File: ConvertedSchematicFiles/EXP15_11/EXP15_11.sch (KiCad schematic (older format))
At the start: 17 parts, among them U5 uA741

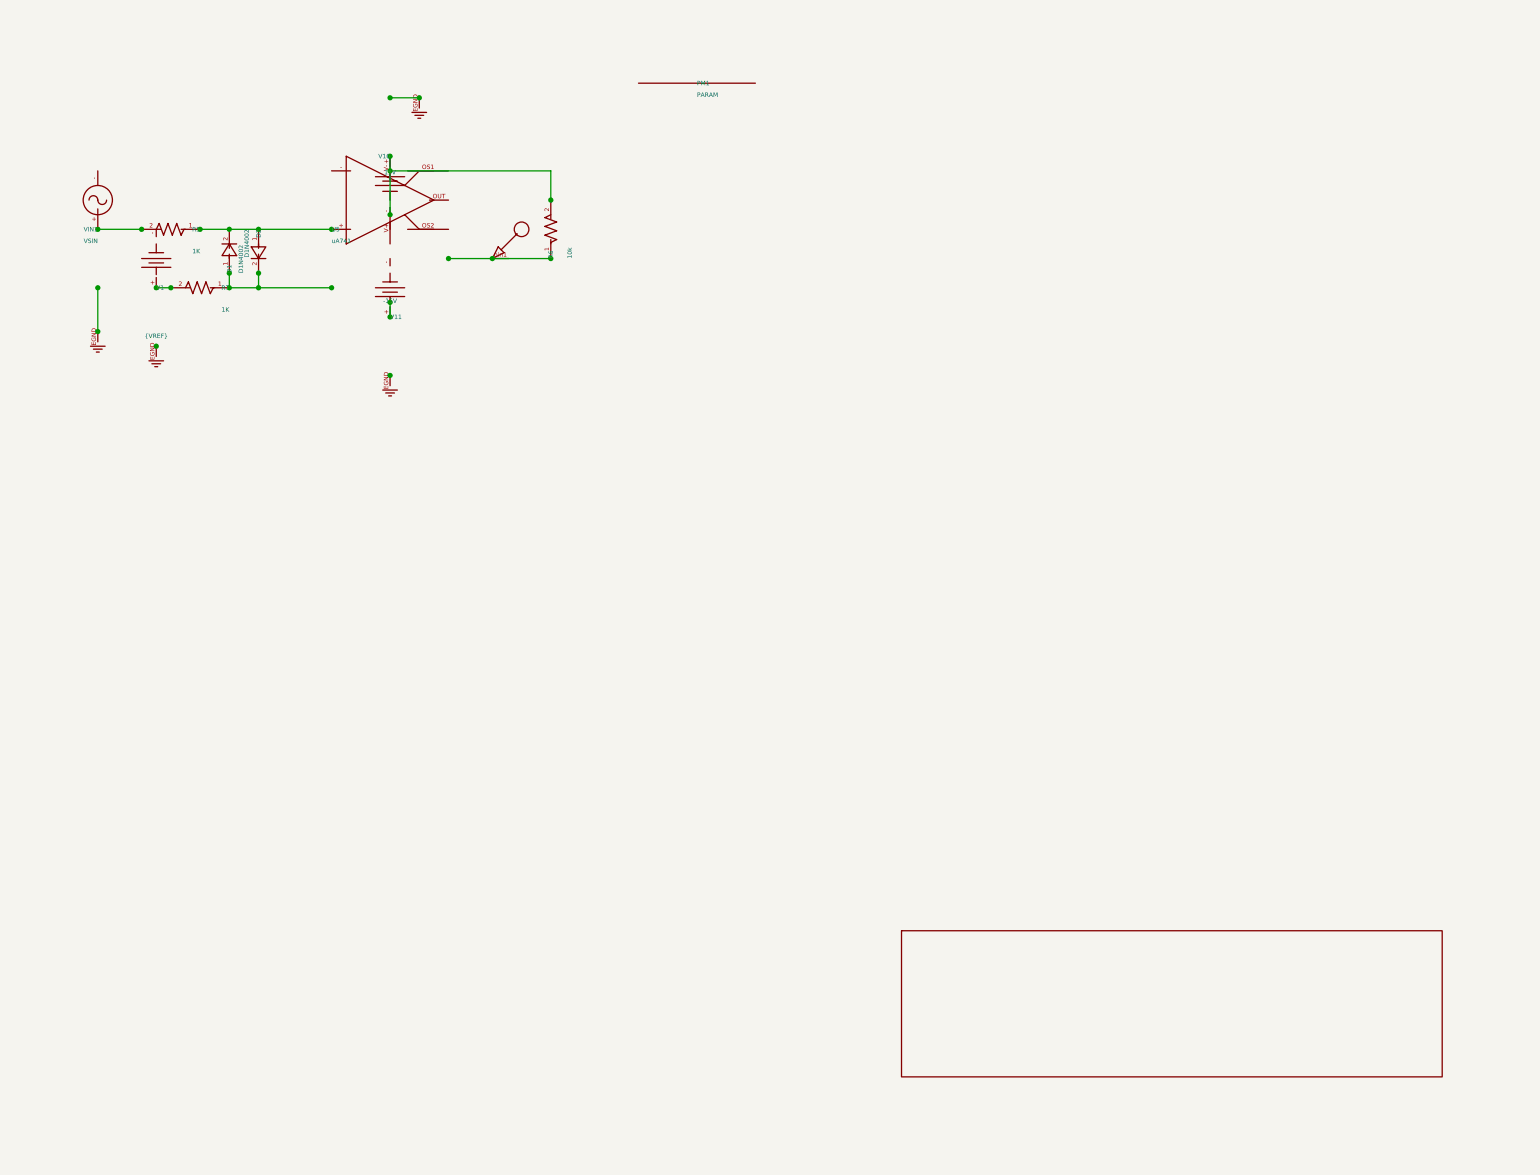
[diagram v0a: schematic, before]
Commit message: Excluded some components. These no longer appear after conversion. When calling shell commands, filenames are in "quotes"
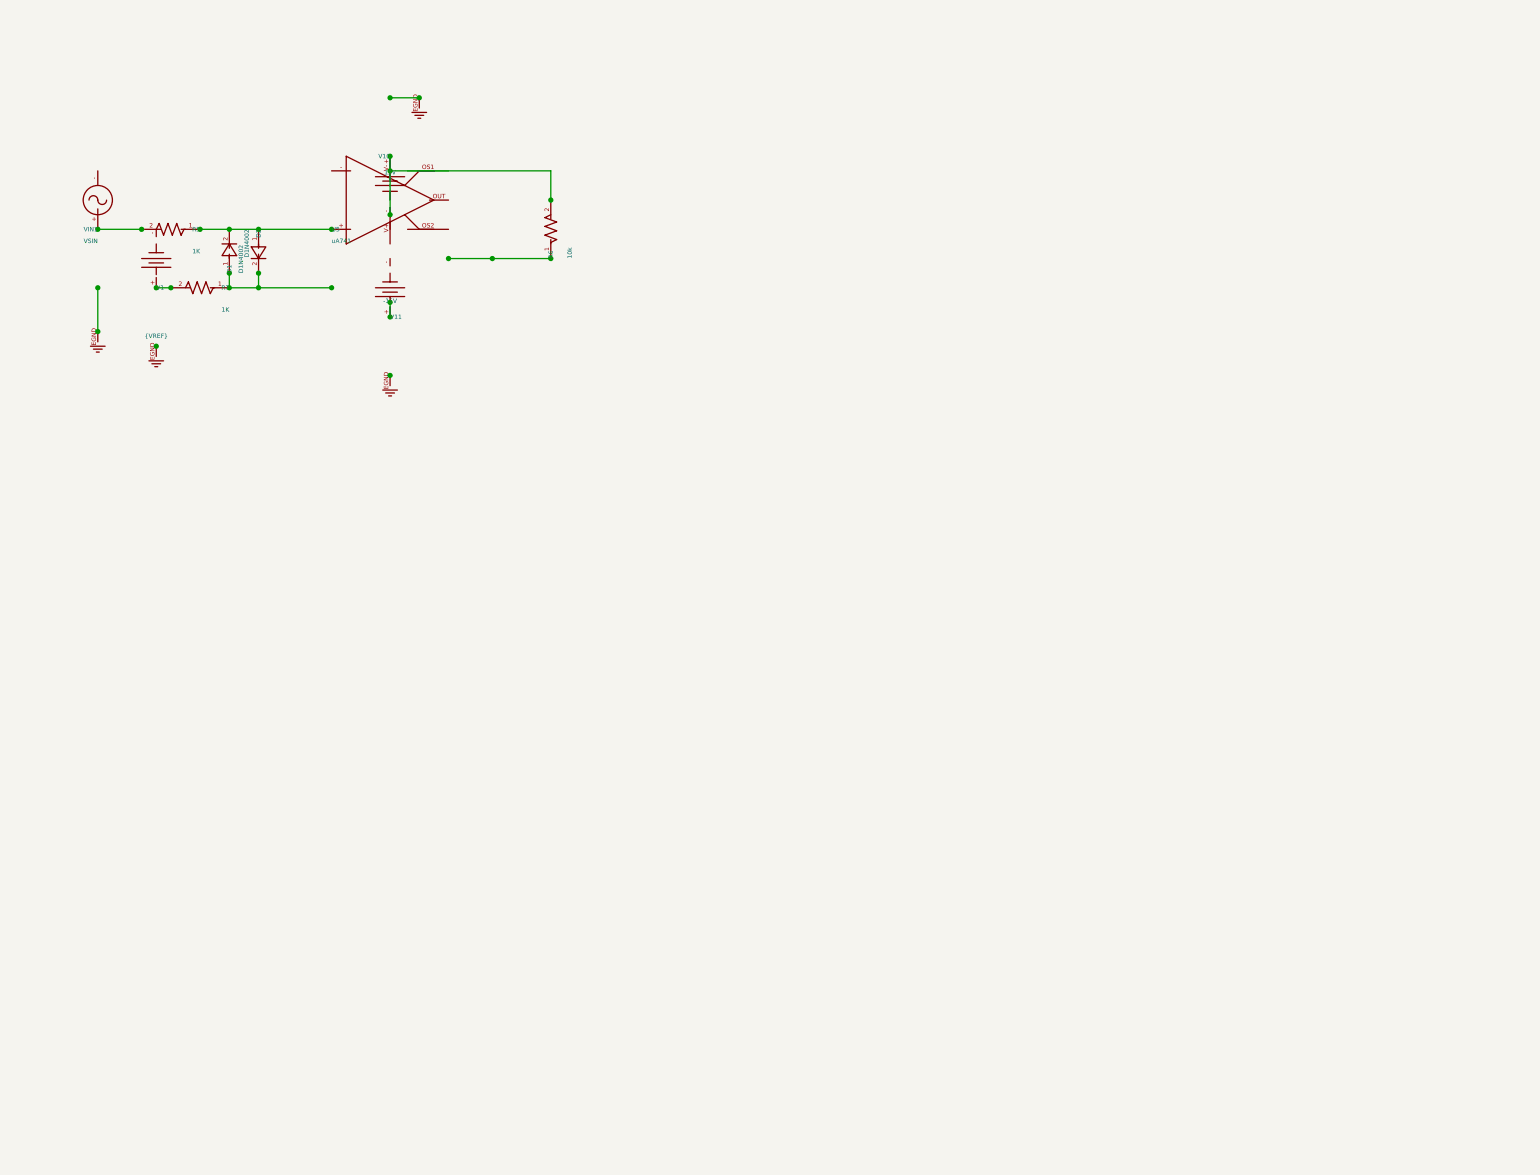
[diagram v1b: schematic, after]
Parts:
- removed PM1: PARAM, symbol PARAM_PSPICE
- removed nodeMarker: nodeMarker, symbol NODEMARKER_PSPICE
- removed titleblk: titleblk, symbol TITLEBLK_PSPICE
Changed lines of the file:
@@
 	0    -1    1    0
-$EndComp
-$Comp
-L PARAM_PSPICE PM1
-U 1 1 74897763
-P 4600 400
-F 0 "PM1" H 4600 400 30  0000 L CNN
-F 1 "PARAM" H 4600 480 30  0000 L CNN
-	1    4600 400
-	1    0    0    1
-$EndComp
-$Comp
-L TITLEBLK_PSPICE titleblk
-U 1 1 87513926
-P 9700 7200
-F 0 "titleblk" H 19400 14400 30  0001 L CNN
-F 1 "titleblk" H 19400 14480 30  0001 L CNN
-	1    9700 7200
-	1    0    0    1
-$EndComp
-$Comp
-L NODEMARKER_PSPICE nodeMarker
-U 1 1 25180540
-P 3200 1600
-F 0 "nodeMarker" H 6400 3200 30  0001 L CNN
-F 1 "nodeMarker" H 6400 3280 30  0001 L CNN
-	1    3200 1600
-	1    0    0    1
 $EndComp
 Wire Wire Line

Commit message: Ports issue fixed. Now annotation for ports is #PWR? function added "itos"
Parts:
- removed EGND (x4): EGND, symbol EGND_PSPICE
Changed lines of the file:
@@
 $EndDescr
 $Comp
-L EGND_PSPICE EGND
+L EGND_PSPICE #PWR1
 U 1 1 14289383
 P 500 2100
-F 0 "EGND" H 1000 4200 30  0001 L CNN
+F 0 "#PWR1" H 1000 4200 30  0001 L CNN
 F 1 "EGND" H 1000 4280 30  0001 L CNN
 	1    500 2100
@@
 $EndComp
 $Comp
-L EGND_PSPICE EGND
+L EGND_PSPICE #PWR2
 U 1 1 46930886
 P 2700 500
-F 0 "EGND" H 5400 1000 30  0001 L CNN
+F 0 "#PWR2" H 5400 1000 30  0001 L CNN
 F 1 "EGND" H 5400 1080 30  0001 L CNN
 	1    2700 500
@@
 $EndComp
 $Comp
-L EGND_PSPICE EGND
+L EGND_PSPICE #PWR3
 U 1 1 71692777
 P 2500 2400
-F 0 "EGND" H 5000 4800 30  0001 L CNN
+F 0 "#PWR3" H 5000 4800 30  0001 L CNN
 F 1 "EGND" H 5000 4880 30  0001 L CNN
 	1    2500 2400
@@
 $EndComp
 $Comp
-L EGND_PSPICE EGND
+L EGND_PSPICE #PWR4
 U 1 1 14636915
 P 900 2200
-F 0 "EGND" H 1800 4400 30  0001 L CNN
+F 0 "#PWR4" H 1800 4400 30  0001 L CNN
 F 1 "EGND" H 1800 4480 30  0001 L CNN
 	1    900 2200

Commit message: Added LICENSE.txt
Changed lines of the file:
@@
 $EndDescr
 $Comp
-L EGND_PSPICE #PWR1
+L GND #PWR1
 U 1 1 14289383
 P 500 2100
@@
 $EndComp
 $Comp
-L EGND_PSPICE #PWR2
+L GND #PWR2
 U 1 1 46930886
 P 2700 500
@@
 $EndComp
 $Comp
-L EGND_PSPICE #PWR3
+L GND #PWR3
 U 1 1 71692777
 P 2500 2400
@@
 $EndComp
 $Comp
-L EGND_PSPICE #PWR4
+L GND #PWR4
 U 1 1 14636915
 P 900 2200

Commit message: Orientation fix. Library components are now inverted, with +ve y axis going up. In Schematic files, +ve y axis is downwards. This is how the KiCad libraries are. As a result of the above fixed, the converted GND is now oriented correctly.
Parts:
- VIN1: value VSIN -> SINE
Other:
- moved on the sheet: U5, V1, V10, V11, VIN1
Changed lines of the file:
@@
 F 1 "EGND" H 1000 4280 30  0001 L CNN
 	1    500 2100
-	-1    0    0    1
+	-1    0    0    -1
 $EndComp
 $Comp
@@
 F 1 "EGND" H 5400 1080 30  0001 L CNN
 	1    2700 500
-	1    0    0    1
+	1    0    0    -1
 $EndComp
 $Comp
@@
 F 1 "EGND" H 5000 4880 30  0001 L CNN
 	1    2500 2400
-	1    0    0    1
+	1    0    0    -1
 $EndComp
 $Comp
@@
 F 1 "EGND" H 1800 4480 30  0001 L CNN
 	1    900 2200
-	1    0    0    1
+	1    0    0    -1
 $EndComp
 $Comp
@@
 F 1 "1K" H 1200 1550 30  0000 L CNN
 	1    1200 1400
-	-1    0    0    1
+	-1    0    0    -1
 $EndComp
 $Comp
@@
 F 1 "10k" H 3600 1730 30  0000 L CNN
 	1    3600 1600
-	0    1    -1    0
+	0    -1    -1    0
 $EndComp
 $Comp
@@
 P 500 1400
 F 0 "VIN1" H 500 1400 30  0000 L CNN
-F 1 "VSIN" H 500 1480 30  0000 L CNN
+F 1 "SINE" H 500 1480 30  0000 L CNN
 	1    500 1400
-	-1    0    0    1
+	-1    0    0    -1
 $EndComp
 $Comp
@@
 F 1 "15V" H 2500 790 30  0000 C CNN
 	1    2500 900
-	-1    0    0    -1
+	-1    0    0    1
 $EndComp
 $Comp
@@
 F 1 "uA741" H 2100 1480 30  0000 L CNN
 	1    2100 1400
-	1    0    0    1
+	1    0    0    -1
 $EndComp
 $Comp
@@
 F 1 "-15V" H 2500 1890 30  0000 C CNN
 	1    2500 2000
-	1    0    0    1
+	1    0    0    -1
 $EndComp
 $Comp
@@
 F 1 "{VREF}" H 900 2130 30  0000 C CNN
 	1    900 1800
-	1    0    0    1
+	1    0    0    -1
 $EndComp
 $Comp
@@
 F 1 "1K" H 1400 1950 30  0000 L CNN
 	1    1400 1800
-	-1    0    0    1
+	-1    0    0    -1
 $EndComp
 $Comp
@@
 F 1 "D1N4002" H 1400 1780 30  0000 L CNN
 	1    1400 1700
-	0    1    -1    0
+	0    -1    -1    0
 $EndComp
 $Comp
@@
 F 1 "D1N4002" H 1600 1480 30  0000 L CNN
 	1    1600 1400
-	0    -1    1    0
+	0    1    1    0
 $EndComp
 Wire Wire Line

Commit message: Removed the use of exec, wrote basename function, made integration with eSim easier.
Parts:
- added PM1: PARAM, symbol PARAM_PSPICE
- added nodeMarker: nodeMarker, symbol nodeMarker_PSPICE
- added titleblk: titleblk, symbol titleblk_PSPICE
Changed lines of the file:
@@
-EESchema Schematic File Version 2  date Tuesday 22 June 1999 09:12:54 PM IST
+EESchema Schematic File Version 2  date
 LIBS:power
 LIBS:device
@@
 LIBS:contrib
 LIBS:valves
-LIBS:ConvertedSchematicFiles/EXP15_11-cache
 EELAYER 25  0
 EELAYER END
@@
 Sheet 1 1
 Title ""
-Date "22 Jun 1999"
+Date ""
 Rev ""
 Comp ""
@@
 	0    1    1    0
 $EndComp
+$Comp
+L PARAM_PSPICE PM1
+U 1 1 74897763
+P 4600 400
+F 0 "PM1" H 4600 400 30  0000 L CNN
+F 1 "PARAM" H 4600 480 30  0000 L CNN
+	1    4600 400
+	1    0    0    -1
+$EndComp
+$Comp
+L titleblk_PSPICE titleblk
+U 1 1 87513926
+P 9700 7200
+F 0 "titleblk" H 19400 14400 30  0001 L CNN
+F 1 "titleblk" H 19400 14480 30  0001 L CNN
+	1    9700 7200
+	1    0    0    -1
+$EndComp
+$Comp
+L nodeMarker_PSPICE nodeMarker
+U 1 1 25180540
+P 3200 1600
+F 0 "nodeMarker" H 6400 3200 30  0001 L CNN
+F 1 "nodeMarker" H 6400 3280 30  0001 L CNN
+	1    3200 1600
+	1    0    0    -1
+$EndComp
 Wire Wire Line
